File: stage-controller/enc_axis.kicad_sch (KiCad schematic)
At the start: 18 parts, among them U16 TMC4361A-LA

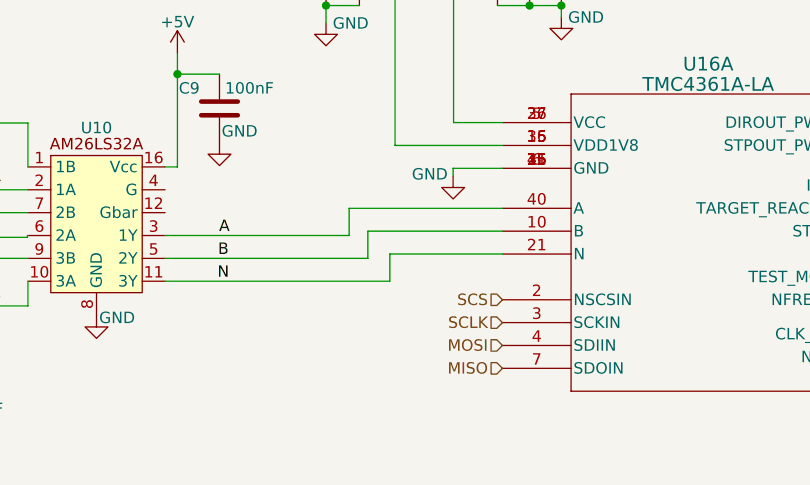
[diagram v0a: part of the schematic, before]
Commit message: Fix Clock pin and MISO/MOSI error
The TeensyCLK signal was routed to a pin on the Teensy 4.1 that did not support PWM. Now fixed. MOSI and MISO of SPI interface were flipped around by mistake. Now in correct orientation and should allow SPI communication (tested with messy wiring).
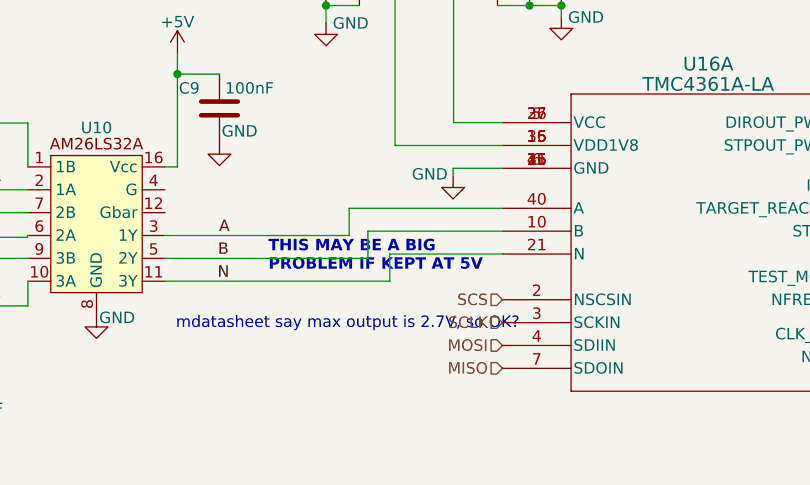
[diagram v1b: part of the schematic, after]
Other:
- note added: "THIS MAY BE A BIG PROBLEM IF KEPT AT 5V"
- note added: "mdatasheet say max output is 2.7V, so OK?"
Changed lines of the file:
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@@
     (effects (font (size 1.27 1.27)) (justify left top))
+  )
+  (text "mdatasheet say max output is 2.7V, so OK?\n" (at 96.393 118.491 0)
+    (effects (font (size 1.27 1.27) (color 255 47 203 1)) (justify left bottom))
+  )
+  (text "THIS MAY BE A BIG\nPROBLEM IF KEPT AT 5V\n" (at 106.68 112.014 0)
+    (effects (font (size 1.27 1.27) (thickness 0.254) bold (color 255 15 51 1)) (justify left bottom))
   )
   (text "Encoder & Tape link" (at 31.242 69.85 0)

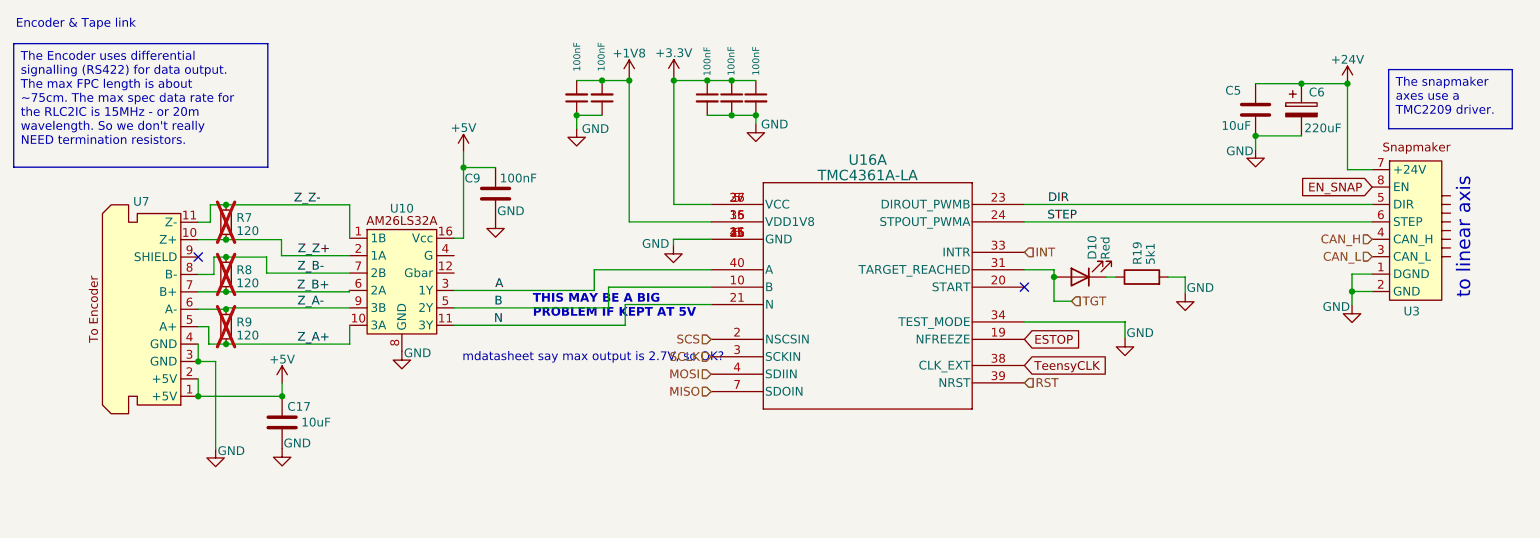
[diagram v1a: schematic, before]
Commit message: Removed differential line receivers
During design of the board I did not realise that the TMC4631 already has this built in (I had different motion controllers before). So the AM26LS32A ICs should not be needed. Removed these and rerouted the board.
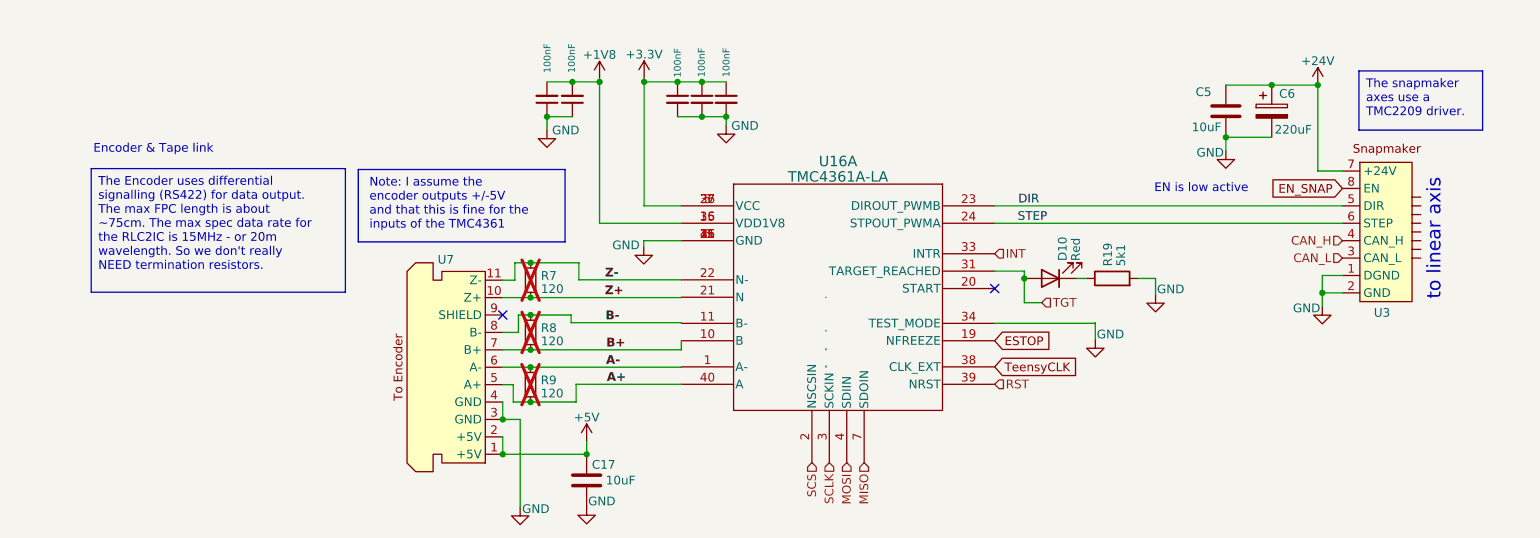
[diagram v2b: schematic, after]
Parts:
- removed C9: 100nF, Capacitor_SMD:C_0603_1608Metric, symbol Device:C
- removed U10: ~, medjed-mainboard:TSSOP-16-AM26LS32A, symbol medjed-mainboard:AM26LS32ACPWR
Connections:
- net Z_A+ is gone; now on net A+: R9.2, U7.5 (A+)
- net Z_B+ is gone; now on net B+: R8.2, U7.7 (B+)
- net Z_Z+ is gone; now on net Z+: R7.2, U7.10 (Z+)
- net A renamed A+
- net B renamed B+
- net N renamed Z+
- net Z_A- renamed A-
- net A-: now also U16.1 (A-)
- net Z_B- renamed B-
- net B-: now also U16.11 (B-)
- net Z_Z- renamed Z-
- net Z-: now also U16.22 (N-)
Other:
- note added: "EN is low active"
- note added: "Note: I assume the encoder outputs +/-5V and that this is fine for the inputs of the TMC4361"
- note removed: "THIS MAY BE A BIG PROBLEM IF KEPT AT 5V"
- note removed: "mdatasheet say max output is 2.7V, so OK?"
- moved on the sheet: C17, C5, C6, D10, R19, R7, R8, R9, U3, U7
